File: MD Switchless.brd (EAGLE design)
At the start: 20 x 14.6 mm, 13 parts, among them U1 ATTINY85-20S

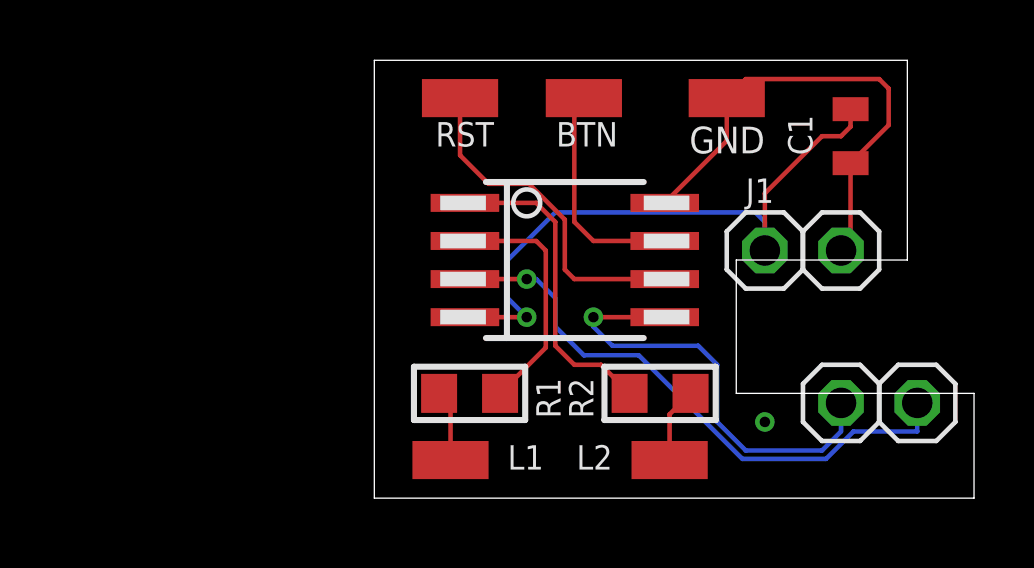
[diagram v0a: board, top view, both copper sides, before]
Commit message: Add files via upload
PCB size and traces width
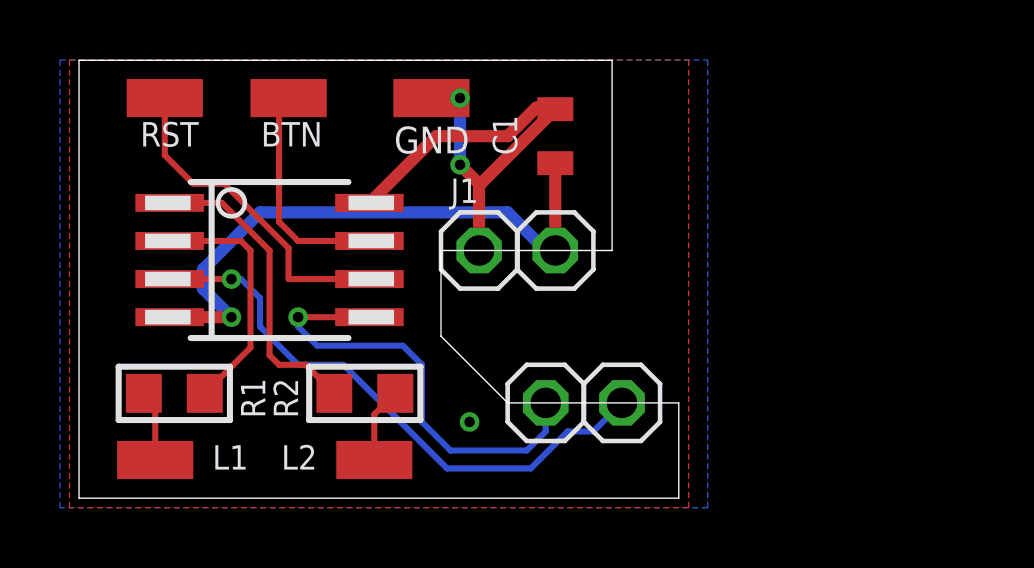
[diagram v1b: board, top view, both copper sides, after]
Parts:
- moved JP2 12.1 mm to (13.3, 8.26)
- moved BTN 9.84 mm to (6.99, 13.3)
- moved C1 9.84 mm to (15.9, 12.1), turned to 90 degrees
- moved JP3 9.84 mm to (18.1, 3.17)
- moved LED1 9.84 mm to (2.54, 1.27)
- moved R1 9.84 mm to (3.17, 3.49)
- moved JP5 9.84 mm to (15.6, 3.17)
- moved LED2 9.84 mm to (9.84, 1.27)
- moved LED3 9.84 mm to (11.7, 13.3)
- moved R2 9.84 mm to (9.53, 3.49)
- moved RST 9.84 mm to (2.86, 13.3)
- moved U1 9.84 mm to (6.35, 7.94)
- moved JP4 6.98 mm to (15.9, 8.26)
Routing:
- net GND: track 16.2 -> 17.4 mm, vias 1 -> 3
- net 5V: track 20.8 -> 20.0 mm
- added copper zone on layer 1, net GND
- added copper zone on layer 16, net GND
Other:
- outline, holes or cut-outs redrawn

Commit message: Add files via upload
minor changes
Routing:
- net 5V: track 20.0 -> 20.8 mm, vias 1 -> 2
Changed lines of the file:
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@@
 <wire x1="9.68" y1="9.8425" x2="11.9025" y2="12.065" width="0.4064" layer="1"/>
 <via x="13.0175" y="2.54" extent="1-16" drill="0.35"/>
-<wire x1="13.335" y1="8.255" x2="13.335" y2="10.425" width="0.4064" layer="1"/>
-<wire x1="13.335" y1="10.425" x2="15.875" y2="12.965" width="0.4064" layer="1"/>
-<wire x1="11.9025" y1="12.065" x2="14.2875" y2="12.065" width="0.4064" layer="1"/>
-<wire x1="14.2875" y1="12.065" x2="15.24" y2="13.0175" width="0.4064" layer="1"/>
-<wire x1="15.24" y1="13.0175" x2="15.8225" y2="13.0175" width="0.4064" layer="1"/>
-<wire x1="15.8225" y1="13.0175" x2="15.875" y2="12.965" width="0.4064" layer="1"/>
-<wire x1="13.335" y1="10.425" x2="13.335" y2="10.4775" width="0.4064" layer="1"/>
-<wire x1="13.335" y1="10.4775" x2="12.7" y2="11.1125" width="0.4064" layer="1"/>
-<via x="12.7" y="11.1125" extent="1-16" drill="0.35"/>
-<wire x1="12.7" y1="11.1125" x2="12.7" y2="13.335" width="0.4064" layer="16"/>
+<wire x1="12.7" y1="13.335" x2="13.335" y2="12.7" width="0.4064" layer="16"/>
 <via x="12.7" y="13.335" extent="1-16" drill="0.35"/>
 <wire x1="12.7" y1="13.335" x2="11.7475" y2="13.335" width="0.4064" layer="1"/>
@@
 <vertex x="-0.635" y="-0.3175"/>
 </polygon>
+<wire x1="15.875" y1="12.965" x2="13.335" y2="10.425" width="0.4064" layer="1"/>
+<wire x1="13.335" y1="10.425" x2="13.335" y2="8.255" width="0.4064" layer="1"/>
+<via x="13.335" y="10.425" extent="1-16" drill="0.35"/>
+<wire x1="13.335" y1="12.7" x2="13.335" y2="10.425" width="0.4064" layer="16"/>
+<wire x1="11.9025" y1="12.065" x2="13.97" y2="12.065" width="0.4064" layer="1"/>
+<wire x1="13.97" y1="12.065" x2="14.9225" y2="13.0175" width="0.4064" layer="1"/>
+<wire x1="14.9225" y1="13.0175" x2="15.8225" y2="13.0175" width="0.4064" layer="1"/>
+<wire x1="15.8225" y1="13.0175" x2="15.875" y2="12.965" width="0.4064" layer="1"/>
+<wire x1="13.0175" y1="2.54" x2="13.335" y2="8.255" width="0" layer="19" extent="1-1"/>
 </signal>
 <signal name="5V" class="2">
@@
 <wire x1="3.02" y1="6.0325" x2="5.08" y2="6.0325" width="0.4064" layer="1"/>
 <via x="5.08" y="6.0325" extent="1-16" drill="0.35"/>
-<wire x1="15.875" y1="8.255" x2="15.5575" y2="8.255" width="0.4064" layer="16"/>
-<wire x1="15.5575" y1="8.255" x2="14.2875" y2="9.525" width="0.4064" layer="16"/>
-<wire x1="14.2875" y1="9.525" x2="6.0325" y2="9.525" width="0.4064" layer="16"/>
+<wire x1="6.0325" y1="9.525" x2="14.2875" y2="9.525" width="0.4064" layer="16"/>
 <wire x1="6.0325" y1="9.525" x2="4.1275" y2="7.62" width="0.4064" layer="16"/>
 <wire x1="4.1275" y1="7.62" x2="4.1275" y2="6.985" width="0.4064" layer="16"/>
 <wire x1="4.1275" y1="6.985" x2="5.08" y2="6.0325" width="0.4064" layer="16"/>
 <wire x1="15.875" y1="8.255" x2="15.875" y2="11.165" width="0.4064" layer="1"/>
+<wire x1="14.2875" y1="9.525" x2="14.605" y2="9.8425" width="0.4064" layer="16"/>
+<via x="14.605" y="9.8425" extent="1-16" drill="0.35"/>
+<wire x1="15.875" y1="11.165" x2="14.9225" y2="11.165" width="0.4064" layer="1"/>
+<wire x1="14.9225" y1="11.165" x2="14.605" y2="10.8475" width="0.4064" layer="1"/>
+<wire x1="14.605" y1="10.8475" x2="14.605" y2="9.8425" width="0.4064" layer="1"/>
 </signal>
 <signal name="LENG">
@@
 <wire x1="2.8575" y1="11.43" x2="3.81" y2="10.4775" width="0.2032" layer="1"/>
 <wire x1="4.8401375" y1="10.4775" x2="6.985" y2="8.3326375" width="0.2032" layer="1"/>
-<wire x1="6.985" y1="8.3326375" x2="6.985" y2="7.3025" width="0.2032" layer="1"/>
-<wire x1="6.985" y1="7.3025" x2="9.68" y2="7.3025" width="0.2032" layer="1"/>
+<wire x1="6.985" y1="8.3326375" x2="6.985" y2="7.62" width="0.2032" layer="1"/>
+<wire x1="6.985" y1="7.62" x2="7.3025" y2="7.3025" width="0.2032" layer="1"/>
+<wire x1="7.3025" y1="7.3025" x2="9.68" y2="7.3025" width="0.2032" layer="1"/>
 <wire x1="3.81" y1="10.4775" x2="4.8401375" y2="10.4775" width="0.2032" layer="1"/>
 </signal>

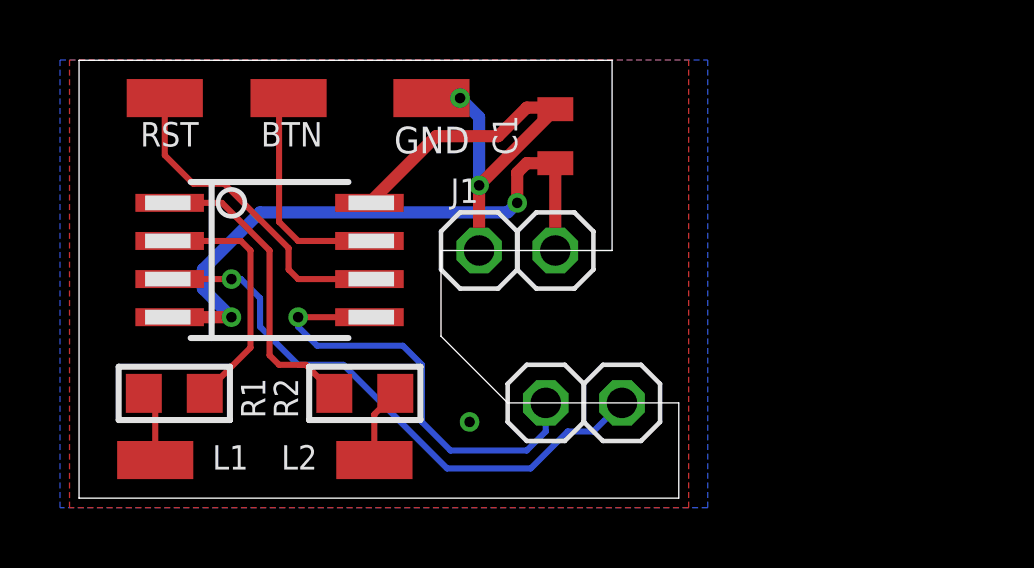
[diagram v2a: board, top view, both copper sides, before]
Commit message: Add files via upload
Wrong position on headers, now it fits perfect
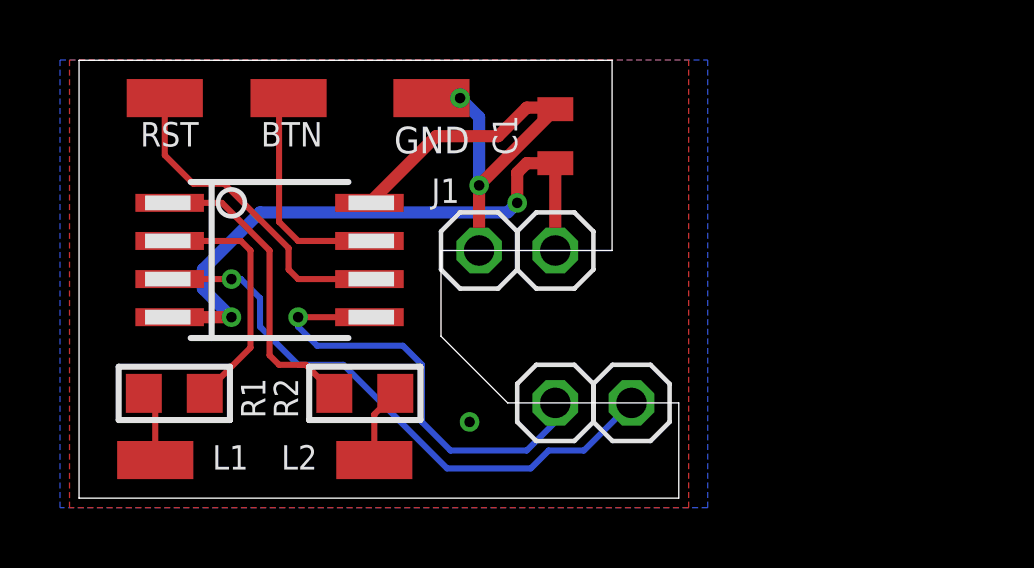
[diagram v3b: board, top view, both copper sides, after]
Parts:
- moved JP5 0.32 mm to (15.9, 3.17)
- moved JP3 0.32 mm to (18.4, 3.17)
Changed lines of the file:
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@@
 <text x="4.445" y="0.9525" size="0.8128" layer="25">L1</text>
 <text x="7.9375" y="0.9525" size="0.8128" layer="25" rot="R180" align="top-left">L2</text>
-<text x="12.3825" y="9.8425" size="0.8128" layer="21">J1</text>
+<text x="11.7475" y="9.8425" size="0.8128" layer="21">J1</text>
 <text x="19.05" y="0.635" size="1.016" layer="22" rot="MR0">designed by @kamencesc</text>
 <text x="0.635" y="0.635" size="1.016" layer="22" rot="MR90">MD Switchless MOD</text>
@@
 <attribute name="VALUE" x="14.605" y="5.08" size="1.27" layer="27"/>
 </element>
-<element name="JP3" library="pinhead" library_urn="urn:adsk.eagle:library:325" package="1X01" package3d_urn="urn:adsk.eagle:package:22485/2" value="" x="18.0975" y="3.175" smashed="yes">
-<attribute name="VALUE" x="16.8275" y="0" size="1.27" layer="27"/>
-</element>
-<element name="JP5" library="pinhead" library_urn="urn:adsk.eagle:library:325" package="1X01" package3d_urn="urn:adsk.eagle:package:22485/2" value="" x="15.5575" y="3.175" smashed="yes">
-<attribute name="VALUE" x="14.2875" y="0" size="1.27" layer="27"/>
+<element name="JP3" library="pinhead" library_urn="urn:adsk.eagle:library:325" package="1X01" package3d_urn="urn:adsk.eagle:package:22485/2" value="" x="18.415" y="3.175" smashed="yes">
+<attribute name="VALUE" x="17.145" y="0" size="1.27" layer="27"/>
+</element>
+<element name="JP5" library="pinhead" library_urn="urn:adsk.eagle:library:325" package="1X01" package3d_urn="urn:adsk.eagle:package:22485/2" value="" x="15.875" y="3.175" smashed="yes">
+<attribute name="VALUE" x="14.605" y="0" size="1.27" layer="27"/>
 </element>
 <element name="U1" library="_hhn_attiny25_45_85" package="SOIC8_EIAJ_208MIL" value="ATTINY85-20S" x="6.35" y="7.9375" smashed="yes" rot="R270"/>
@@
 <wire x1="9.68" y1="6.0325" x2="7.3025" y2="6.0325" width="0.2032" layer="1"/>
 <via x="7.3025" y="6.0325" extent="1-16" drill="0.35"/>
-<wire x1="15.5575" y1="3.175" x2="15.5575" y2="2.2225" width="0.2032" layer="16"/>
-<wire x1="15.5575" y1="2.2225" x2="14.9225" y2="1.5875" width="0.2032" layer="16"/>
+<wire x1="15.875" y1="3.175" x2="15.875" y2="2.54" width="0.2032" layer="16"/>
+<wire x1="15.875" y1="2.54" x2="14.9225" y2="1.5875" width="0.2032" layer="16"/>
 <wire x1="11.43" y1="2.54" x2="11.43" y2="4.445" width="0.2032" layer="16"/>
 <wire x1="11.43" y1="4.445" x2="10.795" y2="5.08" width="0.2032" layer="16"/>
@@
 <wire x1="3.02" y1="7.3025" x2="5.08" y2="7.3025" width="0.2032" layer="1"/>
 <via x="5.08" y="7.3025" extent="1-16" drill="0.35"/>
-<wire x1="18.0975" y1="3.175" x2="17.145" y2="2.2225" width="0.2032" layer="16"/>
-<wire x1="17.145" y1="2.2225" x2="16.2875" y2="2.2225" width="0.2032" layer="16"/>
-<wire x1="16.2875" y1="2.2225" x2="15.0556" y2="0.9906" width="0.2032" layer="16"/>
+<wire x1="18.415" y1="3.175" x2="16.8275" y2="1.5875" width="0.2032" layer="16"/>
+<wire x1="16.8275" y1="1.5875" x2="15.6525" y2="1.5875" width="0.2032" layer="16"/>
+<wire x1="15.6525" y1="1.5875" x2="15.0556" y2="0.9906" width="0.2032" layer="16"/>
 <wire x1="15.0556" y1="0.9906" x2="12.2667625" y2="0.9906" width="0.2032" layer="16"/>
 <wire x1="8.8123625" y1="4.445" x2="7.3025" y2="4.445" width="0.2032" layer="16"/>
